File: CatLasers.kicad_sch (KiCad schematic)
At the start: 0 parts

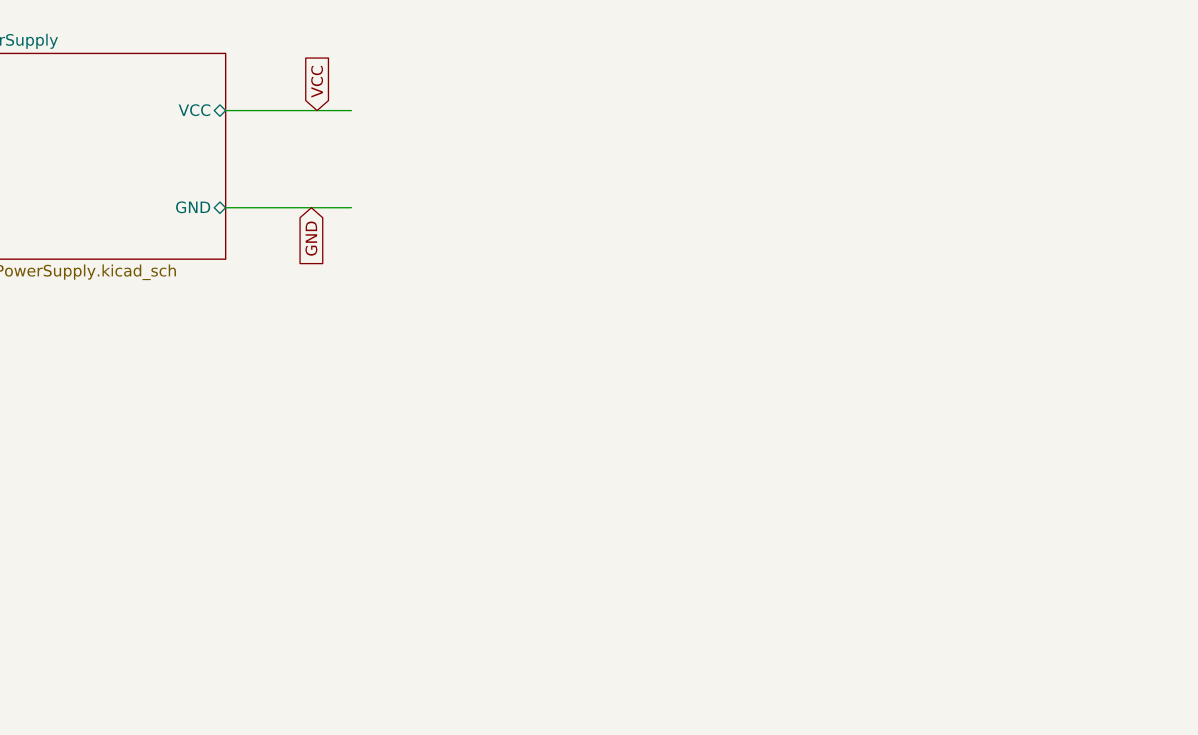
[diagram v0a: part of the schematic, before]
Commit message: 2 voltage regulators + new diodes
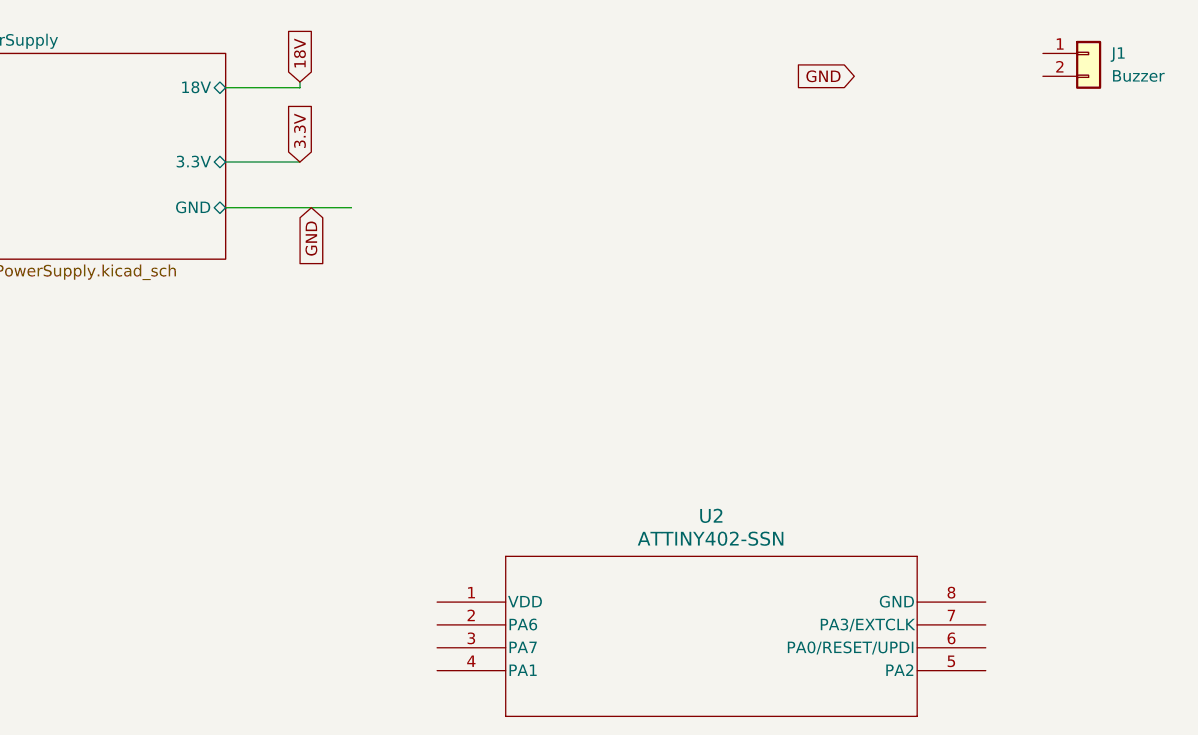
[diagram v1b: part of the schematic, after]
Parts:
- added J1: Buzzer, symbol Connector_Generic:Conn_01x02
- added U2: ATTINY402-SSN, SOIC8_4P9X3P9MC_MCH, symbol ProjMCU:ATTINY402-SSN
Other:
- sheet PowerSupply ports: added 18V, 3.3V; removed VCC
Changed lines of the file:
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@@
 (kicad_sch (version 20230121) (generator eeschema)
   (paper "A4")
+  (wire (pts (xy 80.645 42.545) (xy 80.645 41.91))
+    (stroke (width 0) (type default))
+  )
   (wire (pts (xy 72.39 55.88) (xy 86.36 55.88))
     (stroke (width 0) (type default))
   )
-  (wire (pts (xy 72.39 45.085) (xy 86.36 45.085))
+  (wire (pts (xy 72.39 42.545) (xy 80.645 42.545))
     (stroke (width 0) (type default))
+  )
+  (wire (pts (xy 72.39 50.8) (xy 80.645 50.8))
+    (stroke (width 0) (type default))
+  )
+  (global_label "GND" (shape input) (at 142.24 41.275 180) (fields_autoplaced)
+    (effects (font (size 1.27 1.27)) (justify right))
+    (property "Intersheetrefs" "${INTERSHEET_REFS}" (at 135.3843 41.275 0)
+      (effects (font (size 1.27 1.27)) (justify right) hide)
+    )
   )
   (global_label "GND" (shape input) (at 81.915 55.88 270) (fields_autoplaced)
@@
     )
   )
-  (global_label "VCC" (shape input) (at 82.55 45.085 90) (fields_autoplaced)
+  (global_label "18V" (shape input) (at 80.645 41.91 90) (fields_autoplaced)
     (effects (font (size 1.27 1.27)) (justify left))
-    (property "Intersheetrefs" "${INTERSHEET_REFS}" (at 82.55 38.4712 90)
+    (property "Intersheetrefs" "${INTERSHEET_REFS}" (at 80.645 35.4172 90)
       (effects (font (size 1.27 1.27)) (justify left) hide)
+    )
+  )
+  (global_label "3.3V" (shape input) (at 80.645 50.8 90) (fields_autoplaced)
+    (effects (font (size 1.27 1.27)) (justify left))
+    (property "Intersheetrefs" "${INTERSHEET_REFS}" (at 80.645 43.7024 90)
+      (effects (font (size 1.27 1.27)) (justify left) hide)
+    )
+  )
+  (symbol (lib_id "ProjMCU:ATTINY402-SSN") (at 95.885 99.695 0) (unit 1)
+    (in_bom yes) (on_board yes) (dnp no) (fields_autoplaced)
+    (property "Reference" "U2" (at 126.365 90.17 0)
+      (effects (font (size 1.524 1.524)))
+    )
+    (property "Value" "ATTINY402-SSN" (at 126.365 92.71 0)
+      (effects (font (size 1.524 1.524)))
+    )
+    (property "Footprint" "SOIC8_4P9X3P9MC_MCH" (at 95.885 99.695 0)
+      (effects (font (size 1.27 1.27) italic) hide)
+    )
+    (property "Datasheet" "ATTINY402-SSN" (at 95.885 99.695 0)
+      (effects (font (size 1.27 1.27) italic) hide)
+    )
+    (pin "1")
+    (pin "2")
+    (pin "3")
+    (pin "4")
+    (pin "5")
+    (pin "6")
+    (pin "7")
+    (pin "8")
+    (instances
+      (project "CatLasers"
+        (path "/b94f5b10-ee0c-4425-b025-e3a8bb3cc7b0"
+          (reference "U2") (unit 1)
+        )
+      )
+    )
+  )
+  (symbol (lib_id "Connector_Generic:Conn_01x02") (at 168.275 38.735 0) (unit 1)
+    (in_bom yes) (on_board yes) (dnp no) (fields_autoplaced)
+    (property "Reference" "J1" (at 170.815 38.735 0)
+      (effects (font (size 1.27 1.27)) (justify left))
+    )
+    (property "Value" "Buzzer" (at 170.815 41.275 0)
+      (effects (font (size 1.27 1.27)) (justify left))
+    )
+    (property "Footprint" "" (at 168.275 38.735 0)
+      (effects (font (size 1.27 1.27)) hide)
+    )
+    (property "Datasheet" "~" (at 168.275 38.735 0)
+      (effects (font (size 1.27 1.27)) hide)
+    )
+    (pin "1")
+    (pin "2")
+    (instances
+      (project "CatLasers"
+        (path "/b94f5b10-ee0c-4425-b025-e3a8bb3cc7b0"
+          (reference "J1") (unit 1)
+        )
+      )
     )
   )
@@
       (effects (font (size 1.27 1.27)) (justify left top))
     )
-    (pin "VCC" bidirectional (at 72.39 45.085 0)
-      (effects (font (size 1.27 1.27)) (justify right))
-    )
     (pin "GND" bidirectional (at 72.39 55.88 0)
       (effects (font (size 1.27 1.27)) (justify right))
     )
+    (pin "18V" bidirectional (at 72.39 42.545 0)
+      (effects (font (size 1.27 1.27)) (justify right))
+    )
+    (pin "3.3V" bidirectional (at 72.39 50.8 0)
+      (effects (font (size 1.27 1.27)) (justify right))
+    )

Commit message: Capacitors chosen and footprints assigned
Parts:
- U2: footprint SOIC8_4P9X3P9MC_MCH -> (none)
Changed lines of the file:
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@@
       (effects (font (size 1.524 1.524)))
     )
-    (property "Footprint" "SOIC8_4P9X3P9MC_MCH" (at 95.885 99.695 0)
+    (property "Footprint" "" (at 95.885 99.695 0)
       (effects (font (size 1.27 1.27) italic) hide)
     )

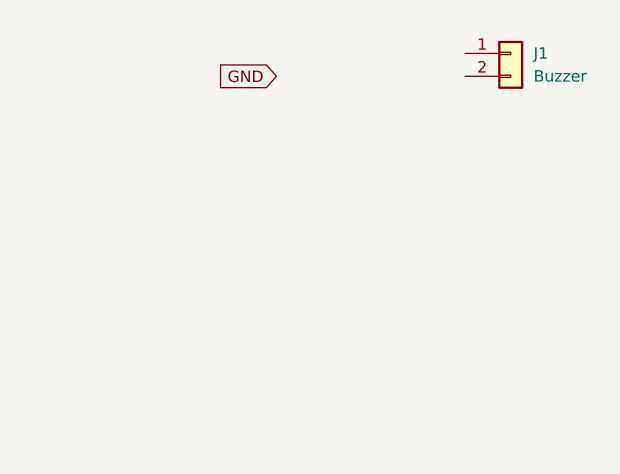
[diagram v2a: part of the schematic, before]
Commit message: Buzzer sheet 1st draft finished
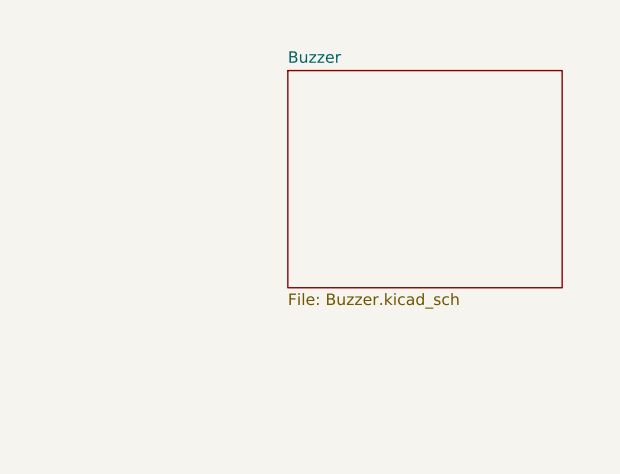
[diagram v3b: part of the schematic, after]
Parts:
- removed J1: Buzzer, symbol Connector_Generic:Conn_01x02
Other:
- added sheet Buzzer (Buzzer.kicad_sch)
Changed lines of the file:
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@@
     (stroke (width 0) (type default))
-  )
-  (global_label "GND" (shape input) (at 142.24 41.275 180) (fields_autoplaced)
-    (effects (font (size 1.27 1.27)) (justify right))
-    (property "Intersheetrefs" "${INTERSHEET_REFS}" (at 135.3843 41.275 0)
-      (effects (font (size 1.27 1.27)) (justify right) hide)
-    )
   )
   (global_label "GND" (shape input) (at 81.915 55.88 270) (fields_autoplaced)
@@
     )
   )
-  (symbol (lib_id "Connector_Generic:Conn_01x02") (at 168.275 38.735 0) (unit 1)
-    (in_bom yes) (on_board yes) (dnp no) (fields_autoplaced)
-    (property "Reference" "J1" (at 170.815 38.735 0)
-      (effects (font (size 1.27 1.27)) (justify left))
-    )
-    (property "Value" "Buzzer" (at 170.815 41.275 0)
-      (effects (font (size 1.27 1.27)) (justify left))
-    )
-    (property "Footprint" "" (at 168.275 38.735 0)
-      (effects (font (size 1.27 1.27)) hide)
-    )
-    (property "Datasheet" "~" (at 168.275 38.735 0)
-      (effects (font (size 1.27 1.27)) hide)
-    )
-    (pin "1")
-    (pin "2")
-    (instances
-      (project "CatLasers"
-        (path "/b94f5b10-ee0c-4425-b025-e3a8bb3cc7b0"
-          (reference "J1") (unit 1)
-        )
-      )
-    )
-  )
   (sheet (at 42.545 38.735) (size 29.845 22.86) (fields_autoplaced)
     (stroke (width 0.1524) (type solid))
@@
       )
     )
+  )
+  (sheet (at 143.51 40.64) (size 30.48 24.13) (fields_autoplaced)
+    (stroke (width 0.1524) (type solid))
+    (fill (color 0 0 0 0.0000))
+    (property "Sheetname" "Buzzer" (at 143.51 39.9284 0)
+      (effects (font (size 1.27 1.27)) (justify left bottom))
+    )
+    (property "Sheetfile" "Buzzer.kicad_sch" (at 143.51 65.3546 0)
+      (effects (font (size 1.27 1.27)) (justify left top))
+    )
+    (instances
+      (project "CatLasers"
+        (path "/b94f5b10-ee0c-4425-b025-e3a8bb3cc7b0" (page "3"))
+      )
+    )

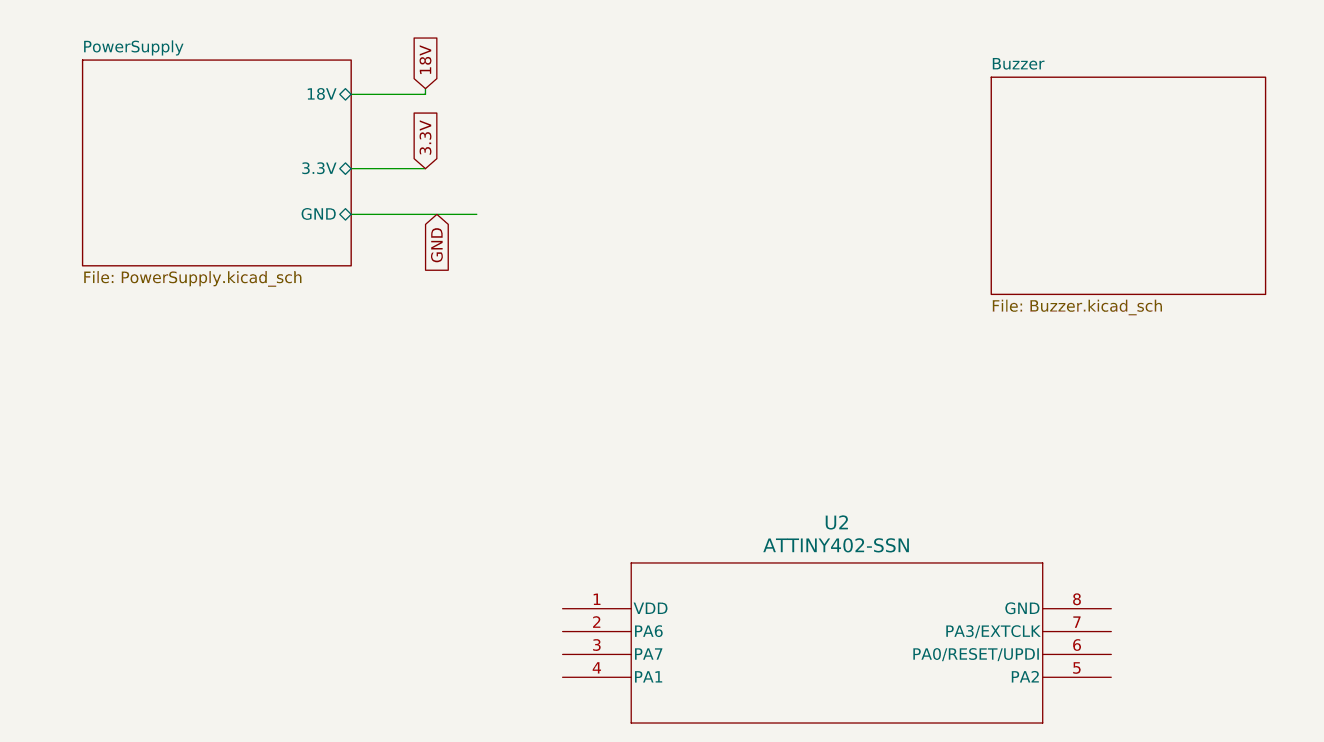
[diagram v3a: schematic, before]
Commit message: MCU Pin Headers added and footprints assigned
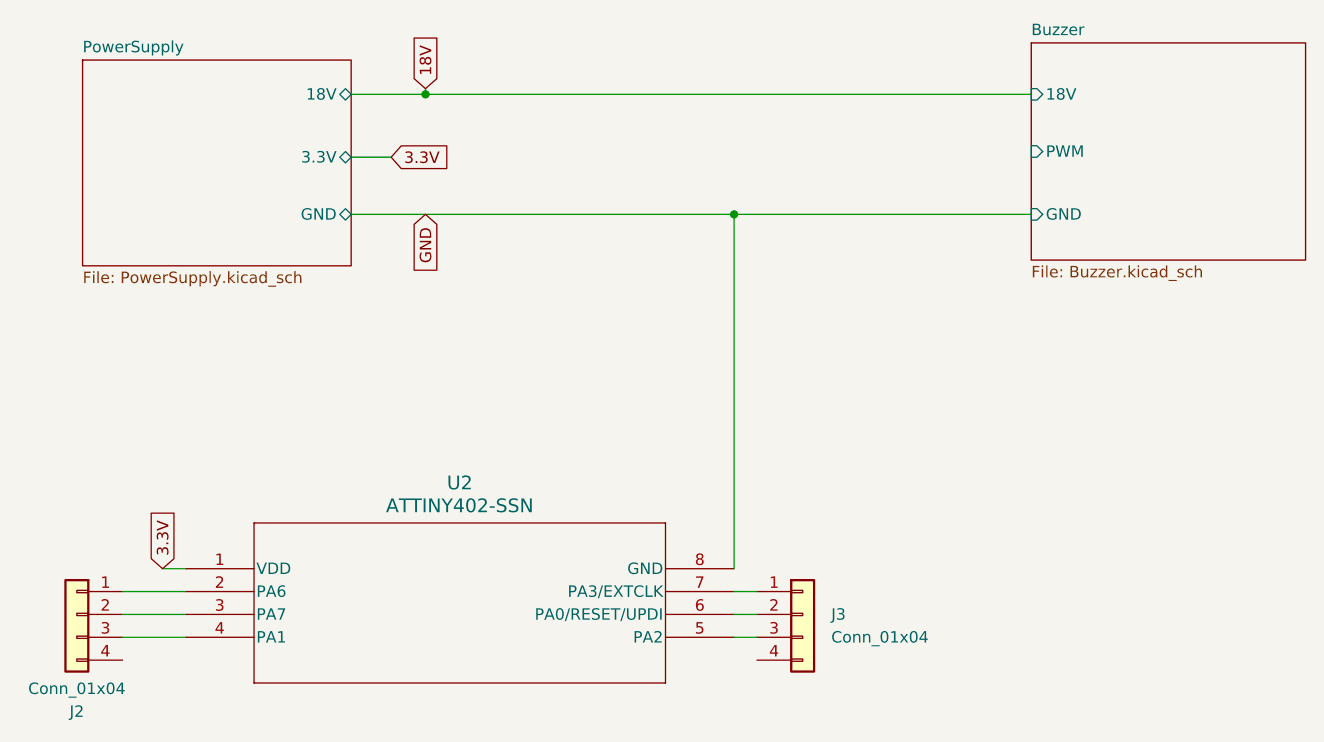
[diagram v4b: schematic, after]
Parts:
- added J2, J3: Conn_01x04, Connector_PinHeader_2.54mm:PinHeader_1x04_P2.54mm_Vertical, symbol Connector_Generic:Conn_01x04
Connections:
- net 3.3V: now also U2.1 (VDD)
- net GND: now also U2.8 (GND)
- net at U2.2 (PA6): now also J2.1 (Pin_1)
- net at U2.3 (PA7): now also J2.2 (Pin_2)
- net at U2.4 (PA1): now also J2.3 (Pin_3)
- net at U2.5 (PA2): now also J3.3 (Pin_3)
- net at U2.6 (PA0/RESET/UPDI): now also J3.2 (Pin_2)
- net at U2.7 (PA3/EXTCLK): now also J3.1 (Pin_1)
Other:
- sheet Buzzer ports: added 18V, GND, PWM; removed none
- moved on the sheet: U2
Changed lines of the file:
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@@
 (kicad_sch (version 20230121) (generator eeschema)
   (paper "A4")
+  (junction (at 80.645 42.545) (diameter 0) (color 0 0 0 0)
+  )
+  (junction (at 114.935 55.88) (diameter 0) (color 0 0 0 0)
+  )
+  (wire (pts (xy 51.435 95.25) (xy 53.975 95.25))
+    (stroke (width 0) (type default))
+  )
+  (wire (pts (xy 114.935 100.33) (xy 117.475 100.33))
+    (stroke (width 0) (type default))
+  )
+  (wire (pts (xy 46.99 102.87) (xy 53.975 102.87))
+    (stroke (width 0) (type default))
+  )
   (wire (pts (xy 80.645 42.545) (xy 80.645 41.91))
     (stroke (width 0) (type default))
   )
-  (wire (pts (xy 72.39 55.88) (xy 86.36 55.88))
+  (wire (pts (xy 114.935 102.87) (xy 117.475 102.87))
+    (stroke (width 0) (type default))
+  )
+  (wire (pts (xy 46.99 97.79) (xy 53.975 97.79))
+    (stroke (width 0) (type default))
+  )
+  (wire (pts (xy 72.39 49.53) (xy 76.835 49.53))
+    (stroke (width 0) (type default))
+  )
+  (wire (pts (xy 80.645 42.545) (xy 147.955 42.545))
     (stroke (width 0) (type default))
   )
@@
     (stroke (width 0) (type default))
   )
-  (wire (pts (xy 72.39 50.8) (xy 80.645 50.8))
+  (wire (pts (xy 114.935 97.79) (xy 117.475 97.79))
     (stroke (width 0) (type default))
   )
-  (global_label "GND" (shape input) (at 81.915 55.88 270) (fields_autoplaced)
+  (wire (pts (xy 72.39 55.88) (xy 114.935 55.88))
+    (stroke (width 0) (type default))
+  )
+  (wire (pts (xy 114.935 55.88) (xy 114.935 95.25))
+    (stroke (width 0) (type default))
+  )
+  (wire (pts (xy 114.935 55.88) (xy 147.955 55.88))
+    (stroke (width 0) (type default))
+  )
+  (wire (pts (xy 46.99 100.33) (xy 53.975 100.33))
+    (stroke (width 0) (type default))
+  )
+  (global_label "3.3V" (shape input) (at 51.435 95.25 90) (fields_autoplaced)
+    (effects (font (size 1.27 1.27)) (justify left))
+    (property "Intersheetrefs" "${INTERSHEET_REFS}" (at 51.435 88.1524 90)
+      (effects (font (size 1.27 1.27)) (justify left) hide)
+    )
+  )
+  (global_label "GND" (shape input) (at 80.645 55.88 270) (fields_autoplaced)
     (effects (font (size 1.27 1.27)) (justify right))
-    (property "Intersheetrefs" "${INTERSHEET_REFS}" (at 81.915 62.7357 90)
+    (property "Intersheetrefs" "${INTERSHEET_REFS}" (at 80.645 62.7357 90)
       (effects (font (size 1.27 1.27)) (justify right) hide)
     )
@@
     )
   )
-  (global_label "3.3V" (shape input) (at 80.645 50.8 90) (fields_autoplaced)
+  (global_label "3.3V" (shape input) (at 76.835 49.53 0) (fields_autoplaced)
     (effects (font (size 1.27 1.27)) (justify left))
-    (property "Intersheetrefs" "${INTERSHEET_REFS}" (at 80.645 43.7024 90)
+    (property "Intersheetrefs" "${INTERSHEET_REFS}" (at 83.9326 49.53 0)
       (effects (font (size 1.27 1.27)) (justify left) hide)
     )
   )
-  (symbol (lib_id "ProjMCU:ATTINY402-SSN") (at 95.885 99.695 0) (unit 1)
+  (symbol (lib_id "ProjMCU:ATTINY402-SSN") (at 53.975 95.25 0) (unit 1)
     (in_bom yes) (on_board yes) (dnp no) (fields_autoplaced)
-    (property "Reference" "U2" (at 126.365 90.17 0)
+    (property "Reference" "U2" (at 84.455 85.725 0)
       (effects (font (size 1.524 1.524)))
     )
-    (property "Value" "ATTINY402-SSN" (at 126.365 92.71 0)
+    (property "Value" "ATTINY402-SSN" (at 84.455 88.265 0)
       (effects (font (size 1.524 1.524)))
     )
-    (property "Footprint" "" (at 95.885 99.695 0)
+    (property "Footprint" "" (at 53.975 95.25 0)
       (effects (font (size 1.27 1.27) italic) hide)
     )
-    (property "Datasheet" "ATTINY402-SSN" (at 95.885 99.695 0)
+    (property "Datasheet" "ATTINY402-SSN" (at 53.975 95.25 0)
       (effects (font (size 1.27 1.27) italic) hide)
     )
@@
         (path "/b94f5b10-ee0c-4425-b025-e3a8bb3cc7b0"
           (reference "U2") (unit 1)
+        )
+      )
+    )
+  )
+  (symbol (lib_id "Connector_Generic:Conn_01x04") (at 41.91 100.33 0) (mirror y) (unit 1)
+    (in_bom yes) (on_board yes) (dnp no)
+    (property "Reference" "J2" (at 41.91 111.125 0)
+      (effects (font (size 1.27 1.27)))
+    )
+    (property "Value" "Conn_01x04" (at 41.91 108.585 0)
+      (effects (font (size 1.27 1.27)))
+    )
+    (property "Footprint" "Connector_PinHeader_2.54mm:PinHeader_1x04_P2.54mm_Vertical" (at 41.91 100.33 0)
+      (effects (font (size 1.27 1.27)) hide)
+    )
+    (property "Datasheet" "~" (at 41.91 100.33 0)
+      (effects (font (size 1.27 1.27)) hide)
+    )
+    (pin "1")
+    (pin "2")
+    (pin "3")
+    (pin "4")
+    (instances
+      (project "CatLasers"
+        (path "/b94f5b10-ee0c-4425-b025-e3a8bb3cc7b0"
+          (reference "J2") (unit 1)
+        )
+      )
+    )
+  )
+  (symbol (lib_id "Connector_Generic:Conn_01x04") (at 122.555 100.33 0) (unit 1)
+    (in_bom yes) (on_board yes) (dnp no) (fields_autoplaced)
+    (property "Reference" "J3" (at 125.73 100.33 0)
+      (effects (font (size 1.27 1.27)) (justify left))
+    )
+    (property "Value" "Conn_01x04" (at 125.73 102.87 0)
+      (effects (font (size 1.27 1.27)) (justify left))
+    )
+    (property "Footprint" "Connector_PinHeader_2.54mm:PinHeader_1x04_P2.54mm_Vertical" (at 122.555 100.33 0)
+      (effects (font (size 1.27 1.27)) hide)
+    )
+    (property "Datasheet" "~" (at 122.555 100.33 0)
+      (effects (font (size 1.27 1.27)) hide)
+    )
+    (pin "1")
+    (pin "2")
+    (pin "3")
+    (pin "4")
+    (instances
+      (project "CatLasers"
+        (path "/b94f5b10-ee0c-4425-b025-e3a8bb3cc7b0"
+          (reference "J3") (unit 1)
         )
       )
@@
       (effects (font (size 1.27 1.27)) (justify right))
     )
-    (pin "3.3V" bidirectional (at 72.39 50.8 0)
+    (pin "3.3V" bidirectional (at 72.39 49.53 0)
       (effects (font (size 1.27 1.27)) (justify right))
     )
@@
     )
   )
-  (sheet (at 143.51 40.64) (size 30.48 24.13) (fields_autoplaced)
+  (sheet (at 147.955 36.83) (size 30.48 24.13) (fields_autoplaced)
     (stroke (width 0.1524) (type solid))
     (fill (color 0 0 0 0.0000))
-    (property "Sheetname" "Buzzer" (at 143.51 39.9284 0)
+    (property "Sheetname" "Buzzer" (at 147.955 36.1184 0)
       (effects (font (size 1.27 1.27)) (justify left bottom))
     )
-    (property "Sheetfile" "Buzzer.kicad_sch" (at 143.51 65.3546 0)
+    (property "Sheetfile" "Buzzer.kicad_sch" (at 147.955 61.5446 0)
       (effects (font (size 1.27 1.27)) (justify left top))
     )
+    (pin "GND" input (at 147.955 55.88 180)
+      (effects (font (size 1.27 1.27)) (justify left))
+    )
+    (pin "PWM" input (at 147.955 48.895 180)
+      (effects (font (size 1.27 1.27)) (justify left))
+    )
+    (pin "18V" input (at 147.955 42.545 180)
+      (effects (font (size 1.27 1.27)) (justify left))
+    )
     (instances
